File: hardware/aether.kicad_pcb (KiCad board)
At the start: 4 copper layers, 100 x 60 mm, 177 parts, among them Q1 S8050_C2146, Q6 AO3401A, U1 USBLC6-2SC6, U10 TPS562201DDCR, U11 TPS562201DDCR, U12 SI5442DU-T1-GE3, U13 BNO086, U14 SI5442DU-T1-GE3, U15 W25Q128JVP, U2 USBLC6-2SC6, U3 SI5442DU-T1-GE3, U4 DPS310, U5 H3LIS331DL, U6 LSM6DSO32TR, U7 SI5442DU-T1-GE3, U8 MS860702BA01-50, U9 SHT45-AD1B-R2, Y1 32.768kHz

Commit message: updated files
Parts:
- removed BZ1: Buzzer, CSS-0575B-SMT:CUI_CSS-0575B-SMT
- removed R17, R18: 10, Resistor_SMD:R_0402_1005Metric
- added BUZ1: FST-5030, FUET-5030:BUZ-SMD_FST-5030, F.Cu at (118.9, 94.1)
- ESP_B0, STM_B0: value SW_SPDT -> SS-3292S-L2-B; footprint Button_Switch_SMD:SW_SPDT_PCM12 -> SS-3292S-L2-B:SW-SMD_SS-3292S-L2-B
- U12, U14, U3, U7: value SI5442DU-T1-GE3 -> SI5448DU-T1-GE3
- moved R32 174.8 mm to (57.2, 133.6)
- moved R30 171.2 mm to (57.2, 125.8)
- moved R31 170.9 mm to (57.2, 127.4)
- moved R29 167.5 mm to (57.2, 119.8)
- moved R33 137.0 mm to (101.7, 106.8)
- moved R34 136.1 mm to (101.7, 107.8)
- moved R23 129.2 mm to (142.5, 92.8), turned to -90 degrees
- moved C13 128.3 mm to (144.0, 101.8), turned to -90 degrees
- moved R13 126.4 mm to (112.2, 113.4), turned to -90 degrees
- moved D1 124.6 mm to (139.6, 87.2)
- moved R5 114.0 mm to (144.2, 112.7), turned to 90 degrees
- moved R2 25.5 mm to (121.2, 98.0)
- moved Q1 22.8 mm to (118.1, 98.8)
- moved LED2 22.1 mm to (120.6, 86.6), turned to 180 degrees
- moved LED1 21.6 mm to (120.6, 88.1), turned to 180 degrees
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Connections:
- ESP32-S3 pad 25: unconnected-(ESP32-S3-IO21-Pad25) -> ESP32-RGB_IN
- ESP32-S3 pad 44: ESP32-RGB_IN -> unconnected-(ESP32-S3-IO46-Pad44)
- ESP_B0 pad 1: ESP32-GPIO0 -> GND
- ESP_B0 pad 2: GND -> ESP32-GPIO0
- STM32F4 pad 15: unconnected-(STM32F4-PA1-Pad15) -> STM32-RGB_IN
- STM32F4 pad 2: STM32-RGB_IN -> unconnected-(STM32F4-PC13-Pad2)
- STM32F4 pad 51: STM32-UART3_TX -> ESP32-RX2
- STM32F4 pad 52: STM32-UART3_RX -> ESP32-TX2
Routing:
- net GND: track 50.4 -> 269.8 mm, vias 12 -> 116
- net GPS_SCL: track 0.00 -> 121.7 mm, vias 0 -> 3
- net GPS_SDA: track 0.00 -> 119.9 mm, vias 0 -> 4
- net 3.3V: track 38.9 -> 148.1 mm, vias 1 -> 51
- net VBUS: track 0.00 -> 104.4 mm, vias 0 -> 12
- net BNO086_MISO: track 0.00 -> 103.2 mm, vias 0 -> 6
- net BNO086_MOSI: track 0.00 -> 100.4 mm, vias 0 -> 5
- net BNO086_SCK: track 0.00 -> 96.6 mm, vias 0 -> 5
- net RFM95W_RST: track 0.00 -> 51.1 mm, vias 0 -> 2
- net ESP32-SPI1_CS0: track 0.00 -> 49.5 mm, vias 0 -> 2
- net ESP32-SPI1_SCK: track 0.00 -> 49.2 mm, vias 0 -> 2
- net ESP32-SPI1_MISO: track 0.00 -> 45.6 mm, vias 0 -> 2
- net ESP32-SPI1_MOSI: track 0.00 -> 45.3 mm, vias 0 -> 2
- net STM32-NRST: track 0.00 -> 37.5 mm, vias 0 -> 2
- net VIN: track 4.00 -> 26.2 mm
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- added copper zone on F.Cu, net PYRO-TERM_A
- added copper zone on F.Cu, net PYRO-TERM_B
- added copper zone on F.Cu, net PYRO-TERM_C
- added copper zone on F.Cu, net PYRO-TERM_D
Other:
- copper layers 4 -> 6
- board text added: "+"
- board text added: "-"
- board text added: "1"
- board text added: "2"
- board text added: "3"
- board text added: "4"
- board text added: "5"
- board text added: "6"
- board text added: "7"
- board text added: "8"
- board text added: "BOOT0"
- board text added: "EN"
- board text added: "ESP32-B0"
- board text added: "GPIO0"
- board text added: "I2C"
- board text added: "NRST"
- board text added: "PYRO"
- board text added: "RADIO"
- board text added: "S"
- board text added: "SPI"
- board text added: "STM32-B0"
- board text added: "UART"
- board text added: "[A]"
- board text added: "[B]"
- board text added: "[C]"
- board text added: "[D]"
- board text added: "∗beep-boop∗"
- board text added: "∗blink∗"
- board text removed: "INT"
- board text removed: "SAFE"

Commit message: rev2 routed
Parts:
- removed the G*** at (140.0, 139.5)
- added G***: LOGO, LOGO, F.Cu at (105.1, 70.1)
- added G***: LOGO, LOGO, F.Cu at (87.6, 57.4)
- added G***: LOGO, LOGO, B.Cu at (90.3, 53.6)
- added G***: LOGO, LOGO, B.Cu at (36.8, 53.1)
- added G***: LOGO, LOGO, B.Cu at (64.6, 52.7)
- added G***: LOGO, LOGO, B.Cu at (65.0, 35.6)
- moved C16 78.3 mm to (71.9, 58.8)
- moved Q1 78.3 mm to (83.0, 28.8)
- moved R19 78.3 mm to (73.4, 67.6)
- moved R20 78.3 mm to (85.1, 67.6)
- moved R6 78.3 mm to (44.9, 67.6)
- moved ANT1 78.3 mm to (29.0, 71.0)
- moved BT1 78.3 mm to (87.8, 32.2)
- moved BUZ1 78.3 mm to (83.9, 24.1)
- moved C1 78.3 mm to (69.4, 52.6)
- moved C10 78.3 mm to (57.1, 48.2)
- moved C11 78.3 mm to (56.6, 49.5)
- moved C12 78.3 mm to (63.8, 64.5)
- moved C13 78.3 mm to (109.0, 31.8)
- moved C14 78.3 mm to (72.5, 64.5)
- moved C15 78.3 mm to (77.0, 40.8)
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- renumbered G*** to G2
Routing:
- net 5V: track 40.1 -> 180.9 mm, vias 4 -> 45
- net STM32-BOOT0: track 0.00 -> 111.3 mm, vias 1 -> 3
- net ESP32-RX1: track 0.00 -> 84.5 mm, vias 1 -> 2
- net ESP32-I2C1_SDA: track 5.24 -> 89.5 mm, vias 1 -> 2
- net ESP32-I2C1_SCL: track 3.01 -> 87.1 mm, vias 1 -> 2
- net ESP32-TX1: track 0.00 -> 80.3 mm, vias 1 -> 2
- net ESP32-GPIO0: track 8.40 -> 85.3 mm, vias 1 -> 3
- net RFM95W_DI0: track 3.33 -> 76.8 mm
- net STM32-UART1_RX: track 0.00 -> 56.4 mm, vias 1 -> 2
- net STM32-UART1_TX: track 0.00 -> 56.2 mm, vias 1 -> 2
- net STM32-I2C2_SDA: track 5.07 -> 58.7 mm, vias 1 -> 2
- net STM32-I2C2_SCL: track 2.98 -> 53.6 mm, vias 1 -> 2
- net ESP32-EN: track 11.9 -> 61.5 mm, vias 1 -> 2
- net STM32-SWDIO: track 2.56 -> 50.4 mm, vias 1 -> 2
- net STM32_USB_D-: track 0.00 -> 47.8 mm, vias 0 -> 2
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- added copper zone on In2.Cu, net 3.3V
- added copper zone on In2.Cu, net 5V
- added copper zone on B.Cu, net GND
- added copper zone on In1.Cu, net GND
- added copper zone on In3.Cu, net GND
- added copper zone on In4.Cu, net GND
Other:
- board text added: "GPS IO"
- board text added: "INT"
- board text added: "PWM"
- board text added: "SAFE"
- board text added: "aether rev 0.2"

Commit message: updated routing
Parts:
- ESPBOOT0: value G -> BLUE
- STMBOOT0: value LED -> BLUE
- moved G*** 0.12 mm to (87.6, 57.2)
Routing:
- net GND: track 270.6 -> 268.5 mm, vias 146 -> 197
- net Net-(U11-SW): track 10.9 -> 11.5 mm
- net 3.3V: track 146.9 -> 147.5 mm
- net BUZZ_IN: track 28.6 -> 28.1 mm
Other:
- board text added: "BATTERY 6-12V"
- board text added: "RADIO ESP32"
- board text added: "RADIO STM32"
- board text removed: "RFD900 ESP32"
- board text removed: "RFD900 STM32"

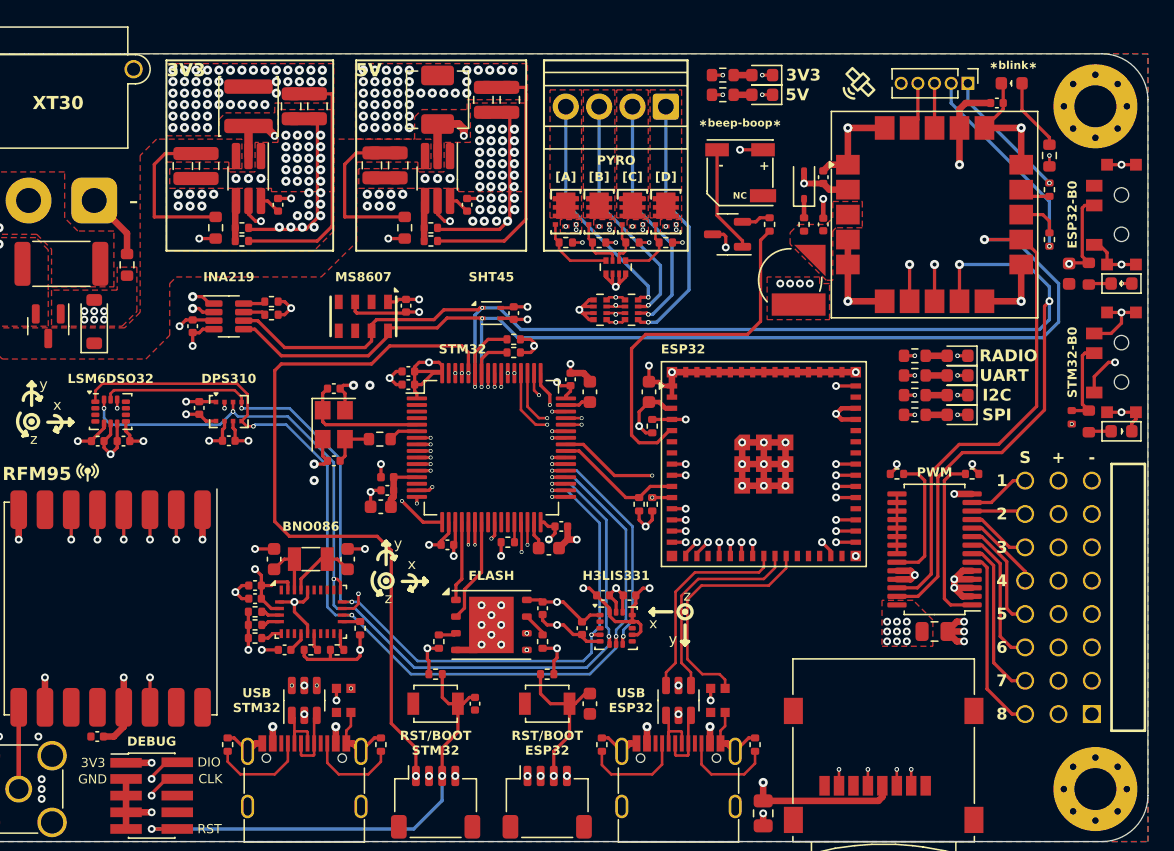
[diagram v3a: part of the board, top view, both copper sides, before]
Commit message: Updated minimum via hole size to 0.3mm.
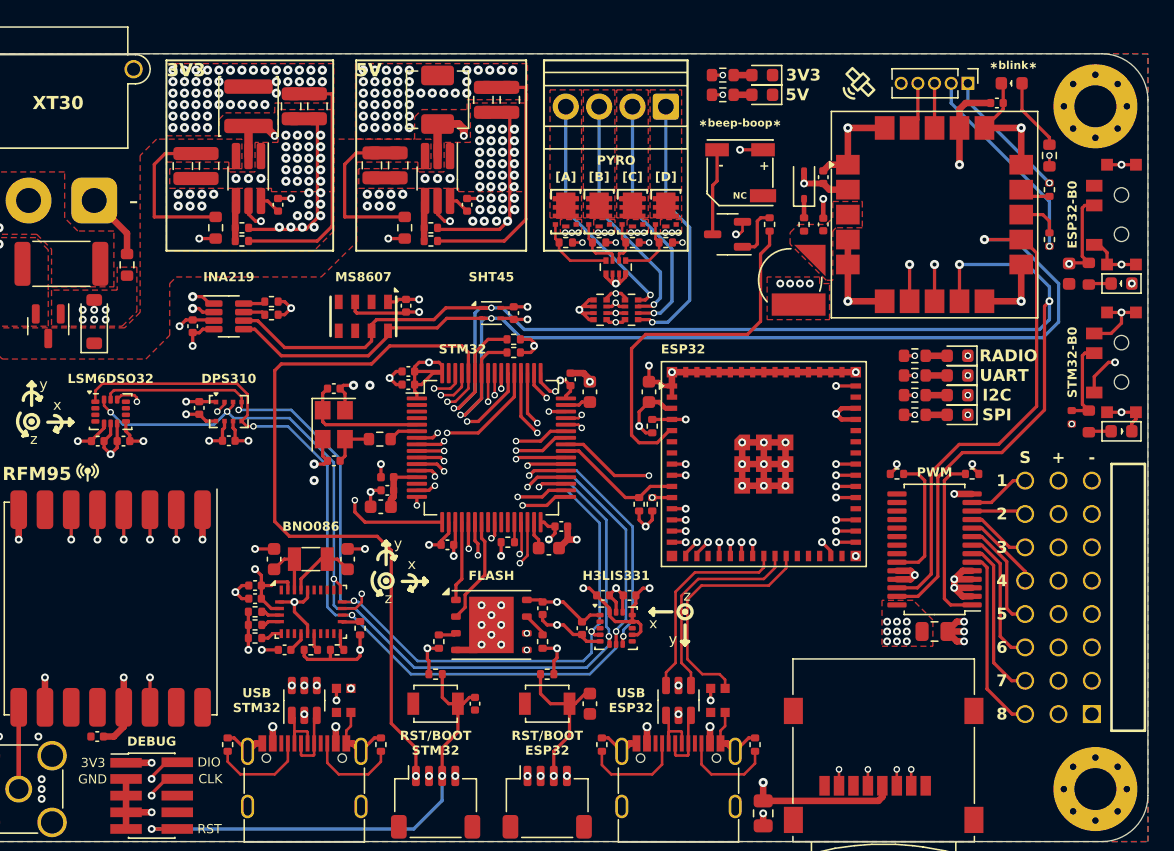
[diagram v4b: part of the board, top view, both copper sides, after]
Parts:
- D4: value LED -> RUBY RED
- D5: value LED -> ROYAL BLUE
- D6: value LED -> EMERALD GREEN
- D7: value LED -> ORANGE
- ESPBOOT0: value BLUE -> G
- R2: value 1k -> 180
- RN3: value 270k -> 220k
- STMBOOT0: value BLUE -> LED
- renumbered RST-BOOT-ESP32 to RST_BOOT_ESP1, RST-BOOT-STM32 to RST_BOOT_STM1
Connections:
- Q1 pad 1: Net-(Q1-C) -> Net-(Q1-B)
- Q1 pad 2: Net-(Q1-B) -> GND
- Q1 pad 3: GND -> Net-(Q1-C)
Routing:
- net PYRO_D: track 21.6 -> 37.1 mm
- net PYRO_C: track 19.6 -> 30.1 mm
- net VBUS: track 99.9 -> 107.5 mm
- net GPS_SCL: track 121.8 -> 128.6 mm
- net BNO086_SCK: track 97.0 -> 103.6 mm
- net GPS_SDA: track 119.9 -> 126.4 mm
- net STM32-BOOT0: track 111.1 -> 117.5 mm
- net PYRO_B: track 19.0 -> 25.2 mm
- net GND: track 268.5 -> 262.4 mm, vias 197 -> 195
- net PYRO_A: track 17.1 -> 22.7 mm
- net BNO086_MOSI: track 101.1 -> 106.1 mm
- net unconnected-(PCA9685-LED10-Pad17): track 4.55 -> 0.00 mm
- net SD_CS: track 43.5 -> 47.3 mm
- net H3LIS331DL_CS: track 18.2 -> 22.0 mm
- net Net-(Q1-B): track 2.12 -> 4.15 mm
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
